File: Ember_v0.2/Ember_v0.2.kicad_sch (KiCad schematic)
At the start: 93 parts, among them J3 DROGUE, J4 BATT_CONN, J5 MAIN, J6 MAN2, J7 DROGUE2, J8 ARM, Q1 SISA96DN-T1, Q2 SISA96DN-T1, Q3 SISA96DN-T1, Q4 SISA96DN-T1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

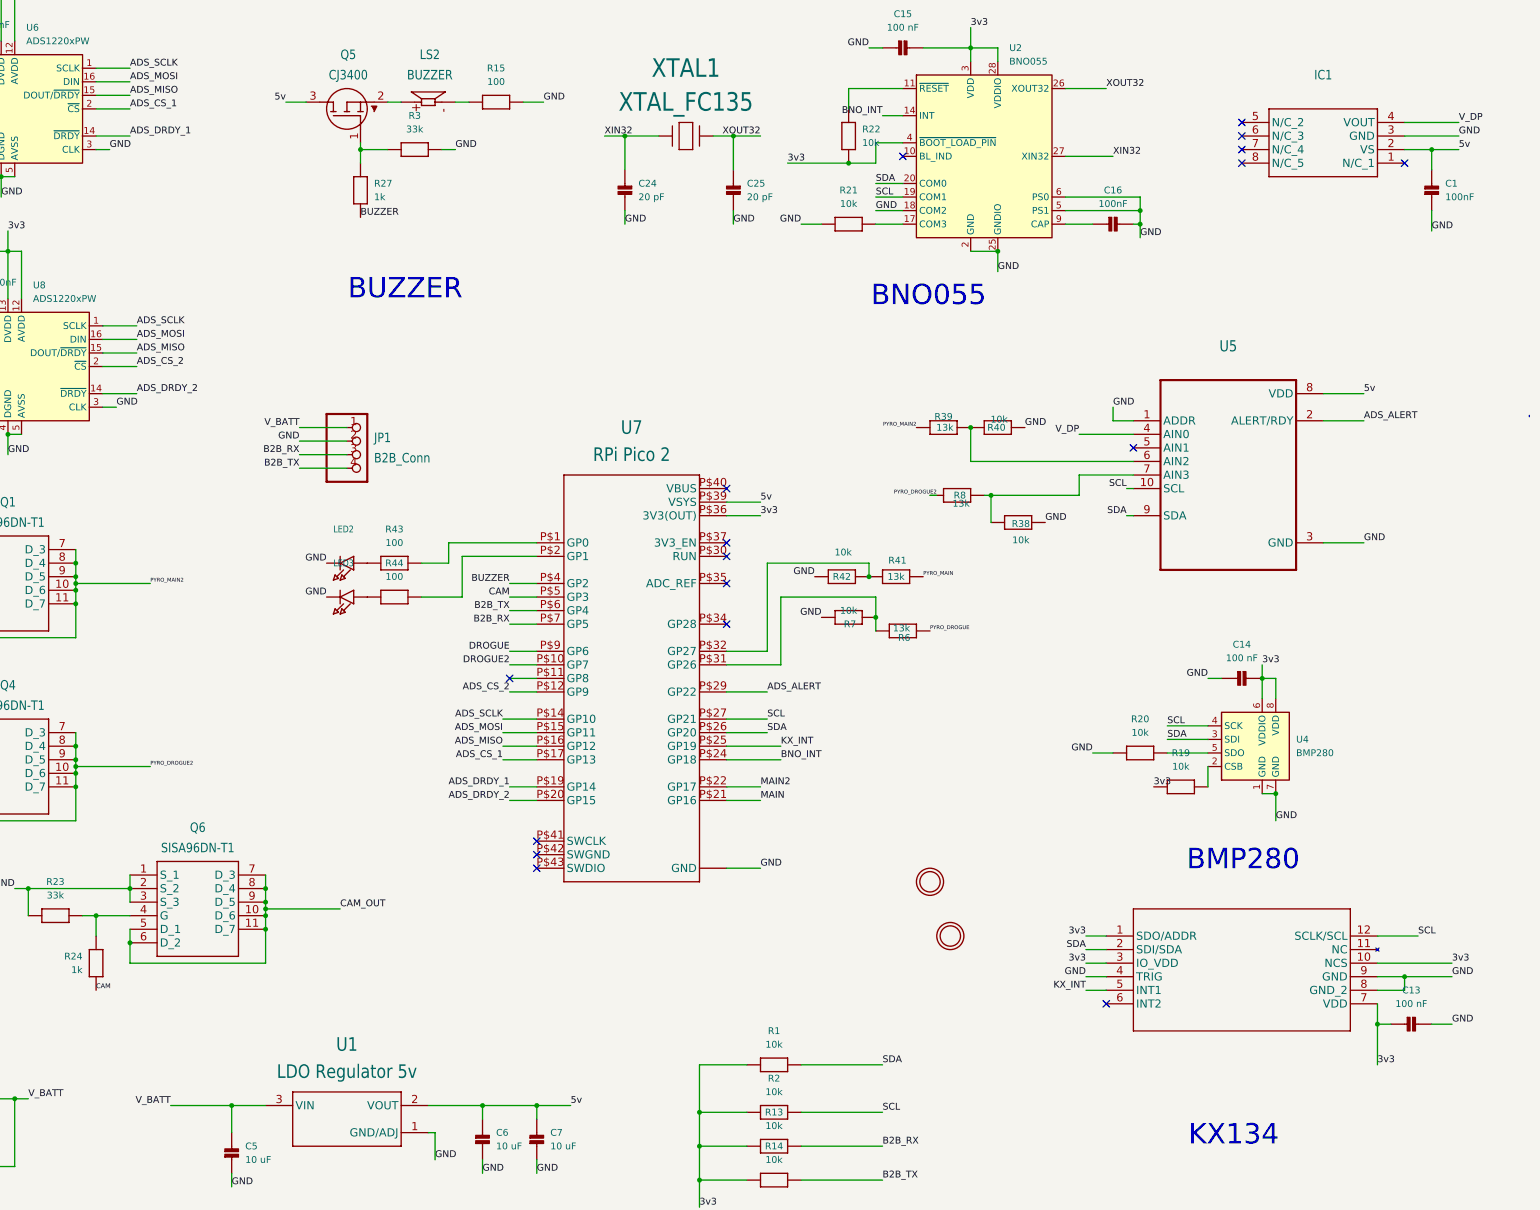
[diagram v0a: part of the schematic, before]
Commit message: All relevant DRC errors are resolved
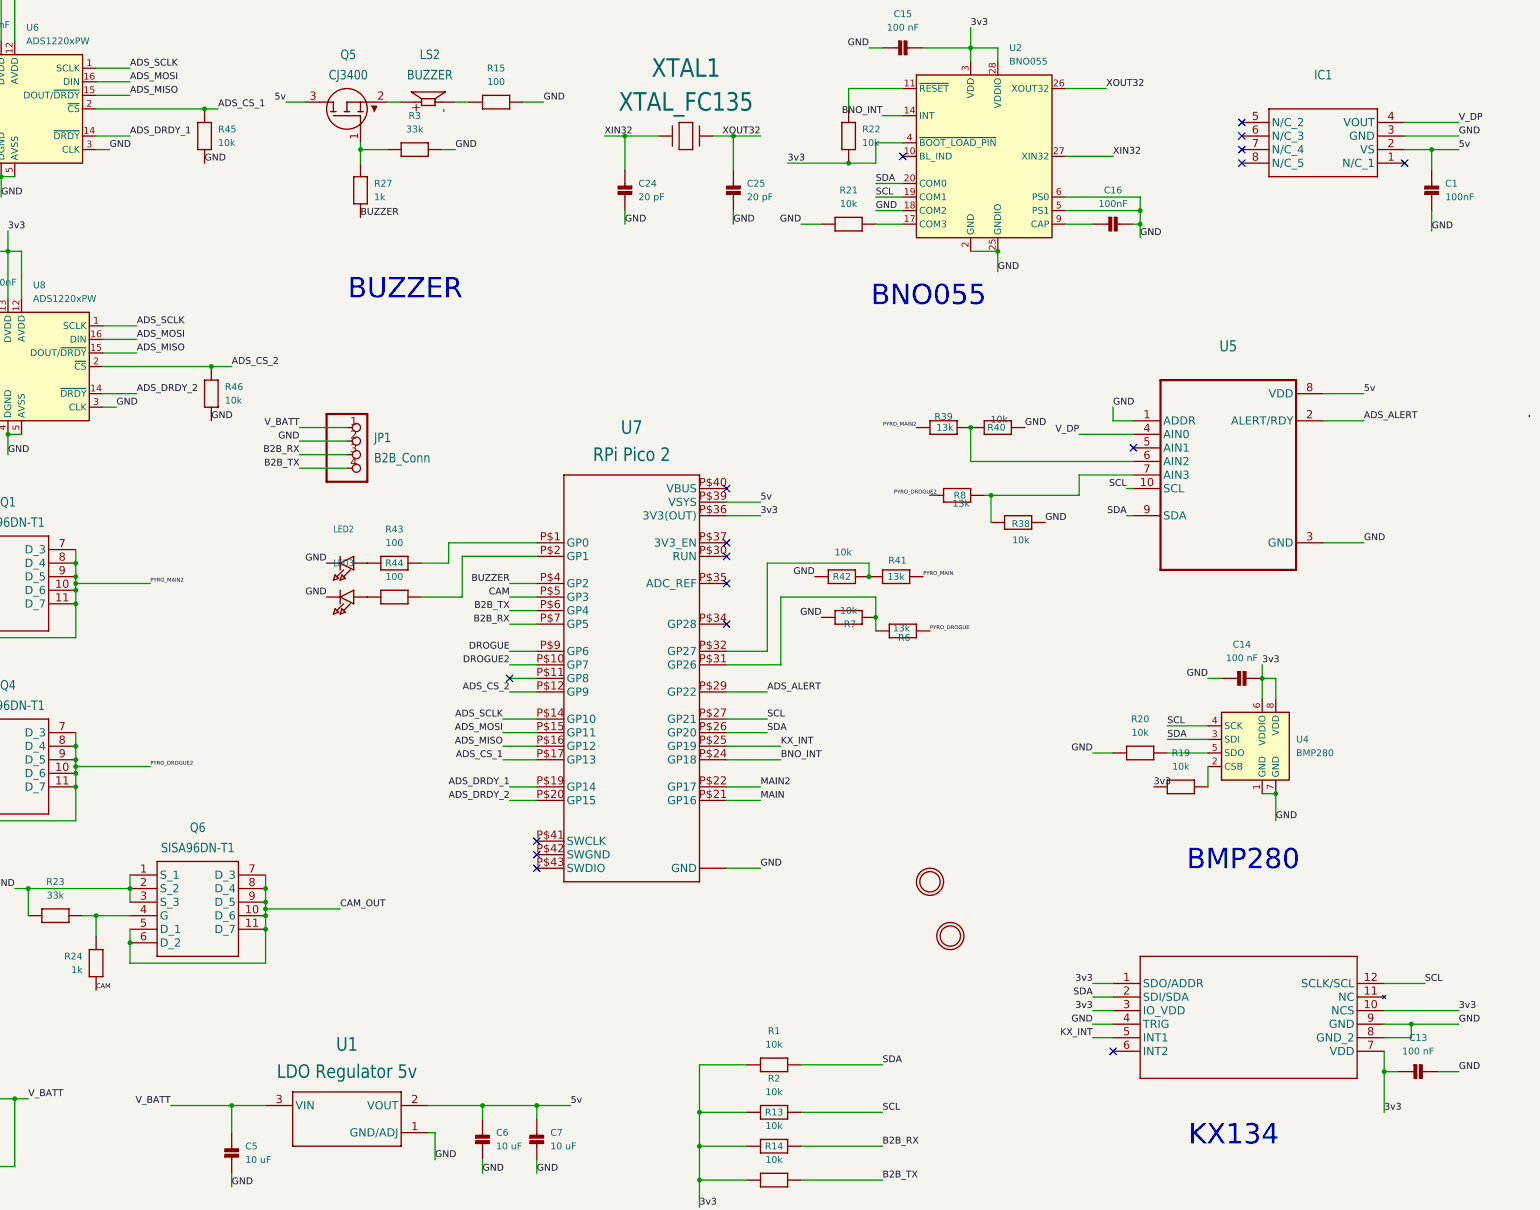
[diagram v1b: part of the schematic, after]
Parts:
- added R45, R46: 10k, microbuilder:0603, symbol microbuilder:RESISTOR0603
- renumbered 11111111111111111 to 111111111111111111, 12111111111111111 to 121111111111111111
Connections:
- net ADS_CS_1: now also R45.1
- net ADS_CS_2: now also R46.1
- net GND: now also R45.2, R46.2
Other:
- moved on the sheet: C13

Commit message: All routings completed, Lisan Al-gaib!
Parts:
- removed 111111111111111111, 121111111111111111: ~, microbuilder:MOUNTINGHOLE_3.0_PLATED, symbol microbuilder:MOUNTINGHOLE
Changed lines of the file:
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@@
-	)
-	(symbol
-		(lib_id "microbuilder:MOUNTINGHOLE")
-		(at 295.91 194.31 0)
-		(unit 1)
-		(exclude_from_sim no)
-		(in_bom yes)
-		(on_board yes)
-		(dnp no)
-		(fields_autoplaced yes)
-		(property "Reference" "111111111111111111"
-			(at 295.91 194.31 0)
-			(effects
-				(font
-					(size 1.27 1.27)
-				)
-				(hide yes)
-			)
-		)
-		(property "Value" "~"
-			(at 295.91 194.31 0)
-			(effects
-				(font
-					(size 1.27 1.27)
-				)
-				(hide yes)
-			)
-		)
-		(property "Footprint" "microbuilder:MOUNTINGHOLE_3.0_PLATED"
-			(at 295.91 194.31 0)
-			(effects
-				(font
-					(size 1.27 1.27)
-				)
-				(hide yes)
-			)
-		)
-		(property "Datasheet" ""
-			(at 295.91 194.31 0)
-			(effects
-				(font
-					(size 1.27 1.27)
-				)
-				(hide yes)
-			)
-		)
-		(property "Description" "Mounting Hole\n\nFor #2 screws (0.086\"/2.18mm width, 0.094\"/2.4mm hole) use 2.5mm"
-			(at 295.91 194.31 0)
-			(effects
-				(font
-					(size 1.27 1.27)
-				)
-				(hide yes)
-			)
-		)
-		(instances
-			(project ""
-				(path "/97e7889e-e69b-4dc1-9c2e-5339b74b36d3"
-					(reference "111111111111111111")
-					(unit 1)
-				)
-			)
-		)
 	)
 	(symbol
@@
 					(unit 1)
 				)
-			)
-		)
-	)
-	(symbol
-		(lib_id "microbuilder:MOUNTINGHOLE")
-		(at 299.72 204.47 0)
-		(unit 1)
-		(exclude_from_sim no)
-		(in_bom yes)
-		(on_board yes)
-		(dnp no)
-		(fields_autoplaced yes)
-		(property "Reference" "121111111111111111"
-			(at 299.72 204.47 0)
-			(effects
-				(font
-					(size 1.27 1.27)
-				)
-				(hide yes)
-			)
-		)
-		(property "Value" "~"
-			(at 299.72 204.47 0)
-			(effects
-				(font
-					(size 1.27 1.27)
-				)
-				(hide yes)
-			)
-		)
-		(property "Footprint" "microbuilder:MOUNTINGHOLE_3.0_PLATED"
-			(at 299.72 204.47 0)
-			(effects
-				(font
-					(size 1.27 1.27)
-				)
-				(hide yes)
-			)
-		)
-		(property "Datasheet" ""
-			(at 299.72 204.47 0)
-			(effects
-				(font
-					(size 1.27 1.27)
-				)
-				(hide yes)
-			)
-		)
-		(property "Description" "Mounting Hole\n\nFor #2 screws (0.086\"/2.18mm width, 0.094\"/2.4mm hole) use 2.5mm"
-			(at 299.72 204.47 0)
-			(effects
-				(font
-					(size 1.27 1.27)
-				)
-				(hide yes)
-			)
-		)
-		(instances
-			(project ""
-				(path "/97e7889e-e69b-4dc1-9c2e-5339b74b36d3"
-					(reference "121111111111111111")
-					(unit 1)
-				)

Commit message: All changes and things are done in both FCU and TDU - Lisan Al-gaib!
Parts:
- removed JP6: ~, microbuilder:1X02_OVAL, symbol microbuilder:HEADER-1X2
- removed Q6: SISA96DN-T1, SISA96DN-T1-GE3:SIS862DNT1GE3, symbol SISA96DN-T1-GE3:SISA96DN-T1-GE3
- removed R23: 33k, microbuilder:0603, symbol microbuilder:RESISTOR0603
- removed R24: 1k, microbuilder:0603, symbol microbuilder:RESISTOR0603
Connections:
- net CAM: no longer names the net of U7.P$5 (GP3)
- no-connect marks 17 -> 18
